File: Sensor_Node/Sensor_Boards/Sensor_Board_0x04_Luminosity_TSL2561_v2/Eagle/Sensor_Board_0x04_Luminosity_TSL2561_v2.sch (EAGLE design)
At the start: 20 parts, among them J1 M04_SMD_90, J4 ARDUINO_ISP, U1 MIKE-TEMP_TSL2561FN, U2 ATMEGA328P_TQFP, Y1 8MHZ

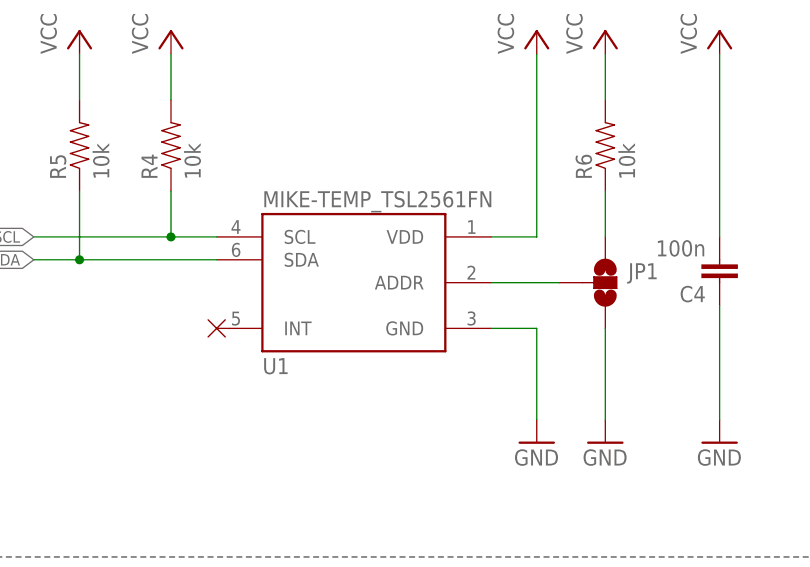
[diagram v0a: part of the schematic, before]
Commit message: Various changes
- updated two masks
- changed combined mask again
- tiedied up CO2 sensor a bit
- used another footprint for TSL2561-sensor
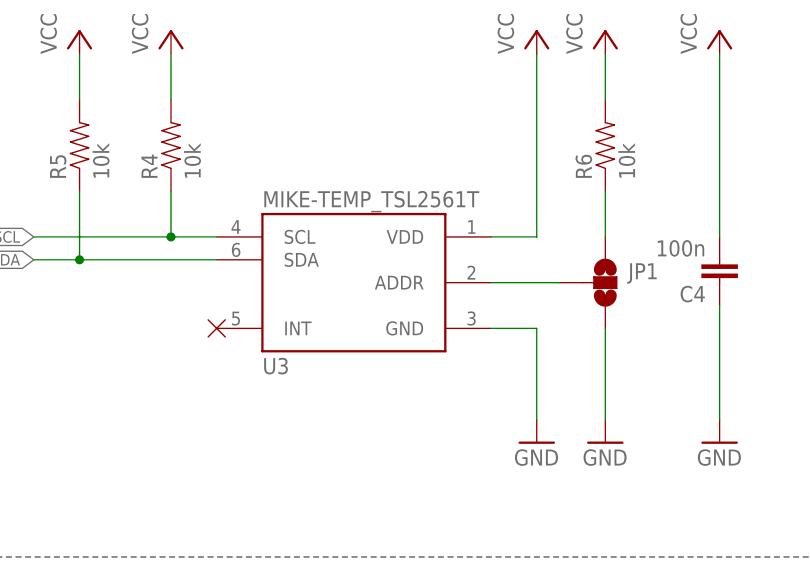
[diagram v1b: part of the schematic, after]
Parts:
- removed U1: MIKE-TEMP_TSL2561FN, TSL2561 Luminosity Sensor BOB:MIKE-TEMP_TSL2561FN
- added U3: MIKE-TEMP_TSL2561T, TSL2561 Luminosity Sensor BOB:MIKE-TEMP_TSL2561T
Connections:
- net GND: now also U3.GND; no longer U1.GND
- net N$7: now also U3.ADDR; no longer U1.ADDR
- net SCL: now also U3.SCL; no longer U1.SCL
- net SDA: now also U3.SDA; no longer U1.SDA
- net VCC: now also U3.VDD; no longer U1.VDD
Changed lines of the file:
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@@
 <?xml version="1.0" encoding="utf-8"?>
 <!DOCTYPE eagle SYSTEM "eagle.dtd">
-<eagle version="8.5.0">
+<eagle version="8.5.2">
 <drawing>
 <settings>
@@
 <part name="U$2" library="myownthings" deviceset="N/C" device=""/>
 <part name="U$10" library="myownthings" deviceset="N/C" device=""/>
-<part name="U1" library="TSL2561 Luminosity Sensor BOB" deviceset="MIKE-TEMP_TSL2561" device="FN"/>
 <part name="R4" library="SparkFun-Passives" deviceset="RESISTOR" device="0805-RES" value="10k"/>
 <part name="R5" library="SparkFun-Passives" deviceset="RESISTOR" device="0805-RES" value="10k"/>
@@
 <part name="GND6" library="SparkFun" deviceset="GND" device=""/>
 <part name="JP1" library="TSL2561 Luminosity Sensor BOB" deviceset="MIKE-TEMP_SOLDERJUMPER_2WAY" device="S"/>
+<part name="U3" library="TSL2561 Luminosity Sensor BOB" deviceset="MIKE-TEMP_TSL2561" device="T"/>
 </parts>
 <sheets>
@@
 <instance part="U$2" gate="G$1" x="99.06" y="177.8"/>
 <instance part="U$10" gate="G$1" x="99.06" y="182.88"/>
-<instance part="U1" gate="G$1" x="180.34" y="162.56"/>
 <instance part="R4" gate="G$1" x="160.02" y="177.8" rot="R90"/>
 <instance part="R5" gate="G$1" x="149.86" y="177.8" rot="R90"/>
@@
 <instance part="GND6" gate="1" x="200.66" y="144.78"/>
 <instance part="JP1" gate="G$1" x="208.28" y="162.56"/>
+<instance part="U3" gate="G$1" x="180.34" y="162.56"/>
 </instances>
 <busses>
@@
 <pinref part="GND6" gate="1" pin="GND"/>
 <wire x1="200.66" y1="147.32" x2="200.66" y2="157.48" width="0.1524" layer="91"/>
-<pinref part="U1" gate="G$1" pin="GND"/>
 <wire x1="200.66" y1="157.48" x2="195.58" y2="157.48" width="0.1524" layer="91"/>
+<pinref part="U3" gate="G$1" pin="GND"/>
 </segment>
 </net>
@@
 </segment>
 <segment>
-<pinref part="U1" gate="G$1" pin="VDD"/>
 <pinref part="P+11" gate="VCC" pin="VCC"/>
 <wire x1="195.58" y1="167.64" x2="200.66" y2="167.64" width="0.1524" layer="91"/>
 <wire x1="200.66" y1="167.64" x2="200.66" y2="187.96" width="0.1524" layer="91"/>
+<pinref part="U3" gate="G$1" pin="VDD"/>
 </segment>
 <segment>
@@
 </segment>
 <segment>
-<pinref part="U1" gate="G$1" pin="SCL"/>
 <pinref part="R4" gate="G$1" pin="1"/>
 <wire x1="165.1" y1="167.64" x2="160.02" y2="167.64" width="0.1524" layer="91"/>
@@
 <junction x="160.02" y="167.64"/>
 <label x="144.78" y="167.64" size="1.27" layer="95" rot="R180" xref="yes"/>
+<pinref part="U3" gate="G$1" pin="SCL"/>
 </segment>
 </net>
@@
 </segment>
 <segment>
-<pinref part="U1" gate="G$1" pin="SDA"/>
 <pinref part="R5" gate="G$1" pin="1"/>
 <wire x1="165.1" y1="165.1" x2="149.86" y2="165.1" width="0.1524" layer="91"/>
@@
 <junction x="149.86" y="165.1"/>
 <label x="144.78" y="165.1" size="1.27" layer="95" rot="R180" xref="yes"/>
+<pinref part="U3" gate="G$1" pin="SDA"/>
 </segment>
 </net>
@@
 <net name="N$7" class="0">
 <segment>
-<pinref part="U1" gate="G$1" pin="ADDR"/>
 <wire x1="195.58" y1="162.56" x2="203.2" y2="162.56" width="0.1524" layer="91"/>
 <pinref part="JP1" gate="G$1" pin="2"/>
-</segment>
-</net>
+<pinref part="U3" gate="G$1" pin="ADDR"/>
+</segment>
+</net>
